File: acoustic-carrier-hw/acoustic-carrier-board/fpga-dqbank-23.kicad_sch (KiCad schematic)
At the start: 32 parts, among them IC1 ECP5-BGA256

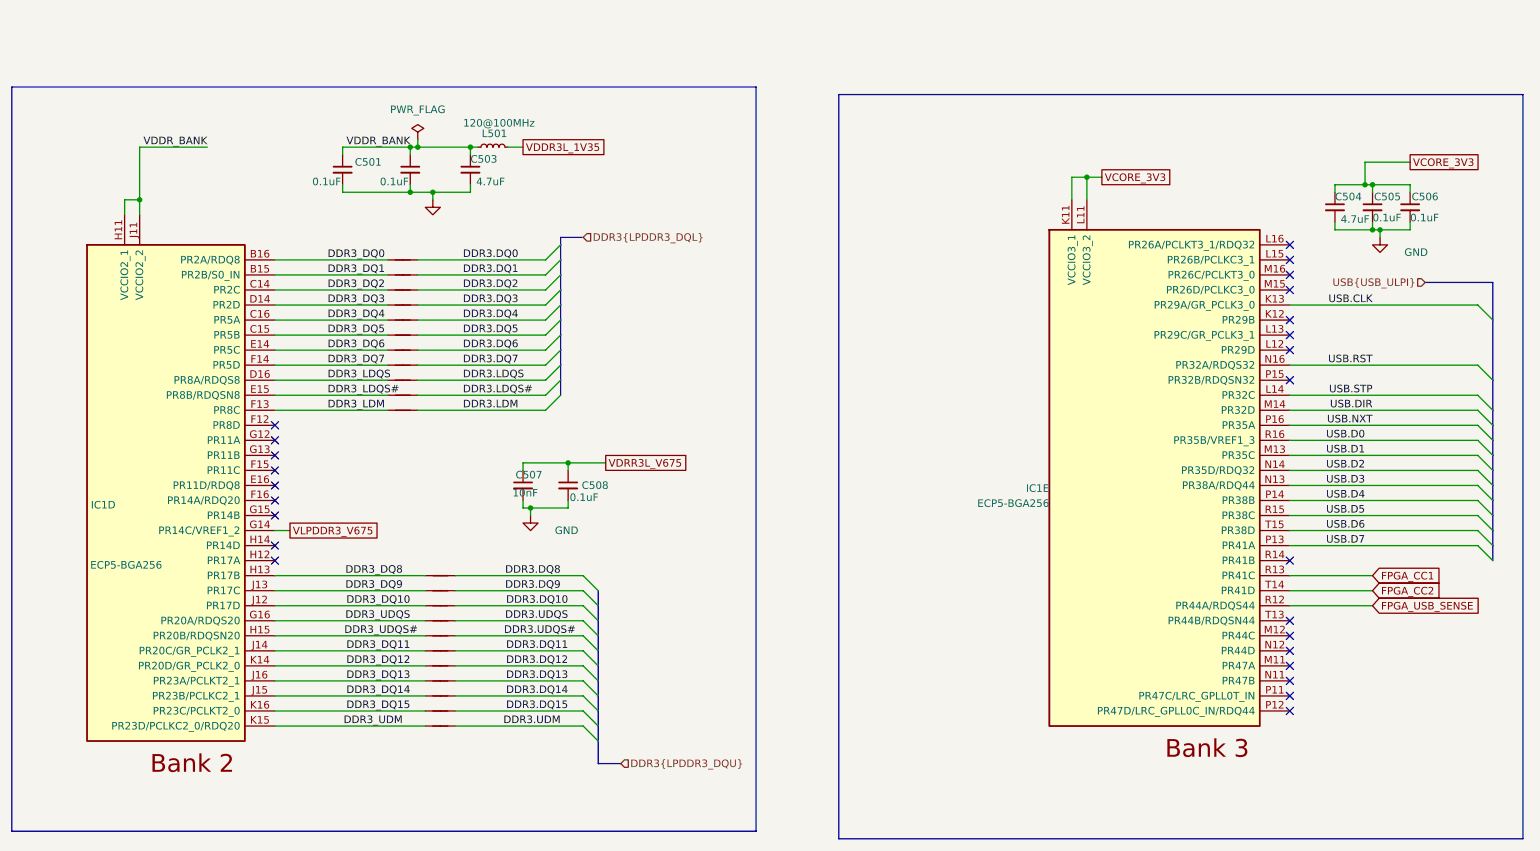
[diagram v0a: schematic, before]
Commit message: [carrier] Removed USB-switch, placed decouplpling for DDR3 and ECP5U (next) consider adding buffers on CC1 and CC2 pins
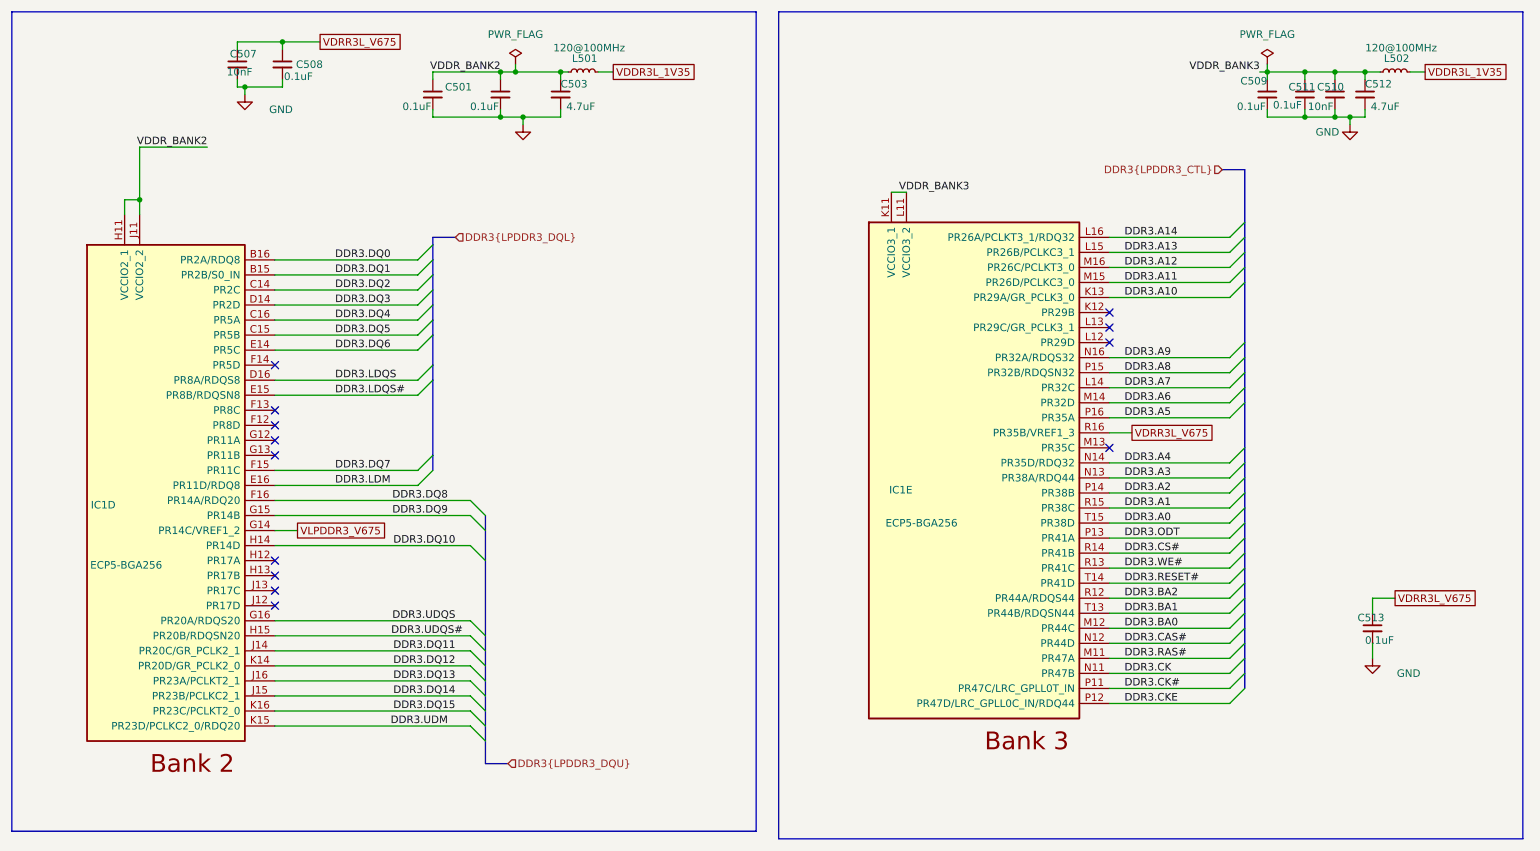
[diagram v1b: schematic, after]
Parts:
- removed C504: 4.7uF, Capacitor_SMD:C_0402_1005Metric, symbol Device:C_Small
- removed C505, C506: 0.1uF, Capacitor_SMD:C_0402_1005Metric, symbol Device:C_Small
- removed NT502, NT503, NT504, NT507, NT508, NT509, NT510, NT511, NT513, NT514, NT515, NT516, NT517, NT518, NT519, NT520, NT523, NT524: NetTie_2, iw-misc:NetTie-2_SMD_Pad0.1565mm, symbol Device:NetTie_2
- removed NT505, NT506, NT521, NT522: NetTie_2, iw-misc:NetTie-2_SMD_Pad0.1240mm, symbol Device:NetTie_2
- added C509, C510, C513: 0.1uF, Capacitor_SMD:C_0201_0603Metric, symbol Device:C_Small
- added C511: 10nF, Capacitor_SMD:C_0201_0603Metric, symbol Device:C_Small
- added C512: 4.7uF, Capacitor_SMD:C_0402_1005Metric, symbol Device:C_Small
- added L502: 120@100MHz, Inductor_SMD:L_0603_1608Metric, symbol Device:L_Small
- C501, C502, C508: footprint Capacitor_SMD:C_0402_1005Metric -> Capacitor_SMD:C_0201_0603Metric; LPN C307331 -> C22435929; MPN CL05B104KB54PNC -> CGA0201X7R104K160ET
- C507: footprint Capacitor_SMD:C_0402_1005Metric -> Capacitor_SMD:C_0201_0603Metric; LPN C15195 -> C285010; MPN CL05B103KB5NNNC -> 0201B103K250NT
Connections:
- net DDR3_DQ0 is gone; now on net DDR3.DQ0: IC1.B16 (PR2A/RDQ8)
- net DDR3_DQ1 is gone; now on net DDR3.DQ1: IC1.B15 (PR2B/S0_IN)
- net DDR3_DQ11 is gone; now on net DDR3.DQ11: IC1.J14 (PR20C/GR_PCLK2_1)
- net DDR3_DQ12 is gone; now on net DDR3.DQ12: IC1.K14 (PR20D/GR_PCLK2_0)
- net DDR3_DQ13 is gone; now on net DDR3.DQ13: IC1.J16 (PR23A/PCLKT2_1)
- net DDR3_DQ14 is gone; now on net DDR3.DQ14: IC1.J15 (PR23B/PCLKC2_1)
- net DDR3_DQ15 is gone; now on net DDR3.DQ15: IC1.K16 (PR23C/PCLKT2_0)
- net DDR3_DQ2 is gone; now on net DDR3.DQ2: IC1.C14 (PR2C)
- net DDR3_DQ3 is gone; now on net DDR3.DQ3: IC1.D14 (PR2D)
- net DDR3_DQ4 is gone; now on net DDR3.DQ4: IC1.C16 (PR5A)
- net DDR3_DQ5 is gone; now on net DDR3.DQ5: IC1.C15 (PR5B)
- net DDR3_DQ6 is gone; now on net DDR3.DQ6: IC1.E14 (PR5C)
- net DDR3_LDQS is gone; now on net DDR3.LDQS: IC1.D16 (PR8A/RDQS8)
- net DDR3_LDQS# is gone; now on net DDR3.LDQS#: IC1.E15 (PR8B/RDQSN8)
- net DDR3_UDM is gone; now on net DDR3.UDM: IC1.K15 (PR23D/PCLKC2_0/RDQ20)
- net DDR3_UDQS is gone; now on net DDR3.UDQS: IC1.G16 (PR20A/RDQS20)
- net DDR3_UDQS# is gone; now on net DDR3.UDQS#: IC1.H15 (PR20B/RDQSN20)
- net USB.D0 is gone; now on net VDRR3L_V675: IC1.R16 (PR35B/VREF1_3)
- net DDR3.DQ10: now also IC1.H14 (PR14D)
- net DDR3.DQ7: now also IC1.F15 (PR11C)
- net DDR3.DQ8: now also IC1.F16 (PR14A/RDQ20)
- net DDR3.DQ9: now also IC1.G15 (PR14B)
- net DDR3.LDM: now also IC1.E16 (PR11D/RDQ8)
- net GND: now also C509.2, C510.2, C511.2, C512.2, C513.2
- net VDDR3L_1V35: now also L502.2
- net VDRR3L_V675: now also C513.1
- net DDR3.A13: now reaches IC1.L15 (PR26B/PCLKC3_1)
- net DDR3.A14: now reaches IC1.L16 (PR26A/PCLKT3_1/RDQ32)
- net DDR3.RAS#: now reaches IC1.M11 (PR47A)
- net DDR3.BA0: now reaches IC1.M12 (PR44C)
- net DDR3.A11: now reaches IC1.M15 (PR26D/PCLKC3_0)
- net DDR3.A12: now reaches IC1.M16 (PR26C/PCLKT3_0)
- net DDR3.CK: now reaches IC1.N11 (PR47B)
- net DDR3.CAS#: now reaches IC1.N12 (PR44D)
- net DDR3.CK#: now reaches IC1.P11 (PR47C/LRC_GPLL0T_IN)
- net DDR3.CKE: now reaches IC1.P12 (PR47D/LRC_GPLL0C_IN/RDQ44)
- net DDR3.A8: now reaches IC1.P15 (PR32B/RDQSN32)
- net DDR3.CS#: now reaches IC1.R14 (PR41B)
- net DDR3.BA1: now reaches IC1.T13 (PR44B/RDQSN44)
- net DDR3_DQ10: no longer names the net of IC1.J12 (PR17D)
- net DDR3_DQ7: no longer names the net of IC1.F14 (PR5D)
- net DDR3_DQ8: no longer names the net of IC1.H13 (PR17B)
- net DDR3_DQ9: no longer names the net of IC1.J13 (PR17C)
- net DDR3_LDM: no longer names the net of IC1.F13 (PR8C)
- net FPGA_CC1 renamed DDR3.WE#
- net FPGA_CC2 renamed DDR3.RESET#
- net FPGA_USB_SENSE renamed DDR3.BA2
- net USB.CLK renamed DDR3.A10
- net USB.D1: no longer names the net of IC1.M13 (PR35C)
- net USB.D2 renamed DDR3.A4
- net USB.D3 renamed DDR3.A3
- net USB.D4 renamed DDR3.A2
- net USB.D5 renamed DDR3.A1
- net USB.D6 renamed DDR3.A0
- net USB.D7 renamed DDR3.ODT
- net USB.DIR renamed DDR3.A6
- net USB.NXT renamed DDR3.A5
- net USB.RST renamed DDR3.A9
- net USB.STP renamed DDR3.A7
- net VCORE_3V3 renamed VDDR_BANK3
- net VDDR_BANK3: now also C509.1, C510.1, C511.1, C512.1, L502.1
- net VDDR_BANK renamed VDDR_BANK2
- no-connect marks 25 -> 13
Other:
- moved on the sheet: C501, C503, C507, C508, IC1E, L501

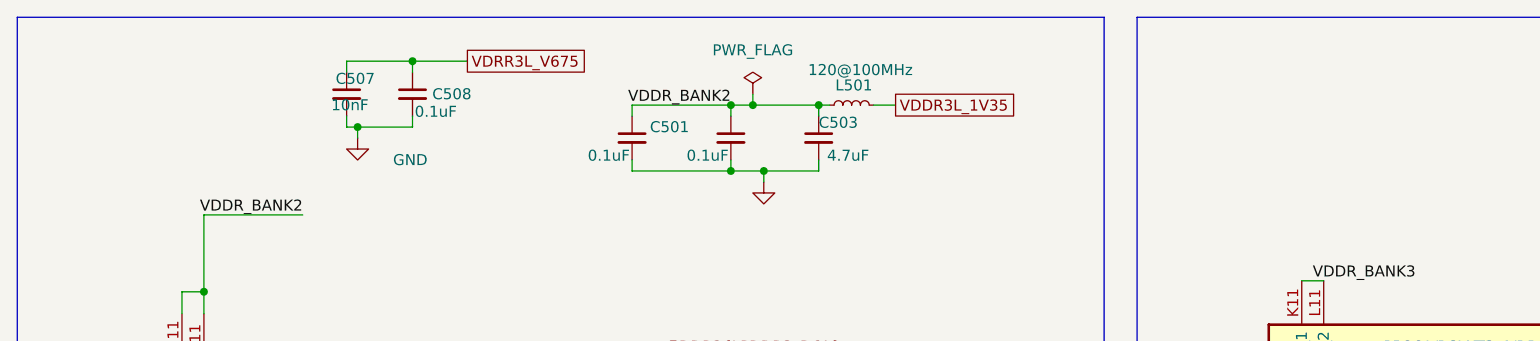
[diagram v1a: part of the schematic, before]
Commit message: [carrier] connected ethernet, usb and adc to appropriate banks, redpositioned schmitt trigger and USB
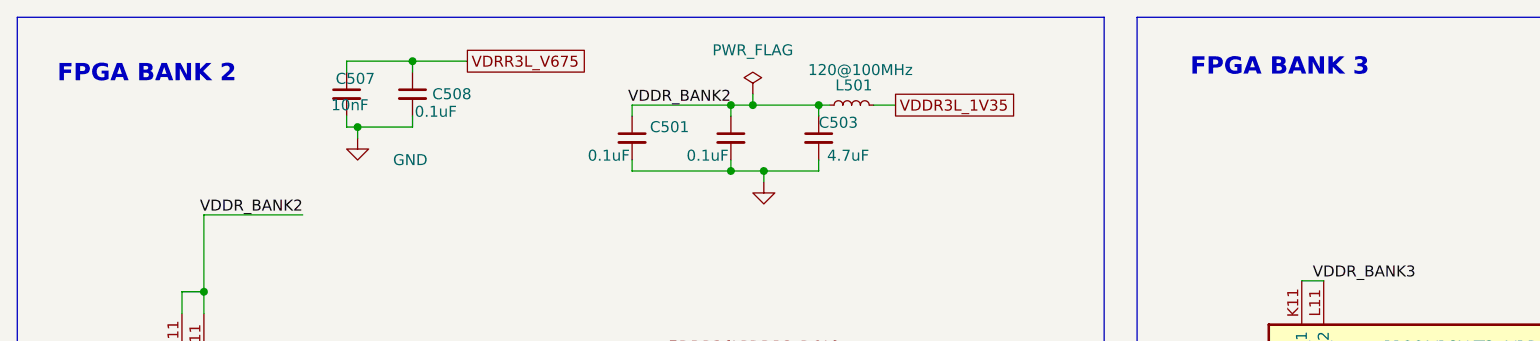
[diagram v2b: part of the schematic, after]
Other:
- note added: "FPGA BANK 2"
- note added: "FPGA BANK 3"
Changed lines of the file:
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@@
+		)
+	)
+	(text "FPGA BANK 3\n"
+		(exclude_from_sim no)
+		(at 172.72 26.162 0)
+		(effects
+			(font
+				(size 2 2)
+				(thickness 0.254)
+				(bold yes)
+			)
+		)
+	)
+	(text "FPGA BANK 2"
+		(exclude_from_sim no)
+		(at 41.656 26.924 0)
+		(effects
+			(font
+				(size 2 2)
+				(thickness 0.254)
+				(bold yes)
+			)
 		)
 	)

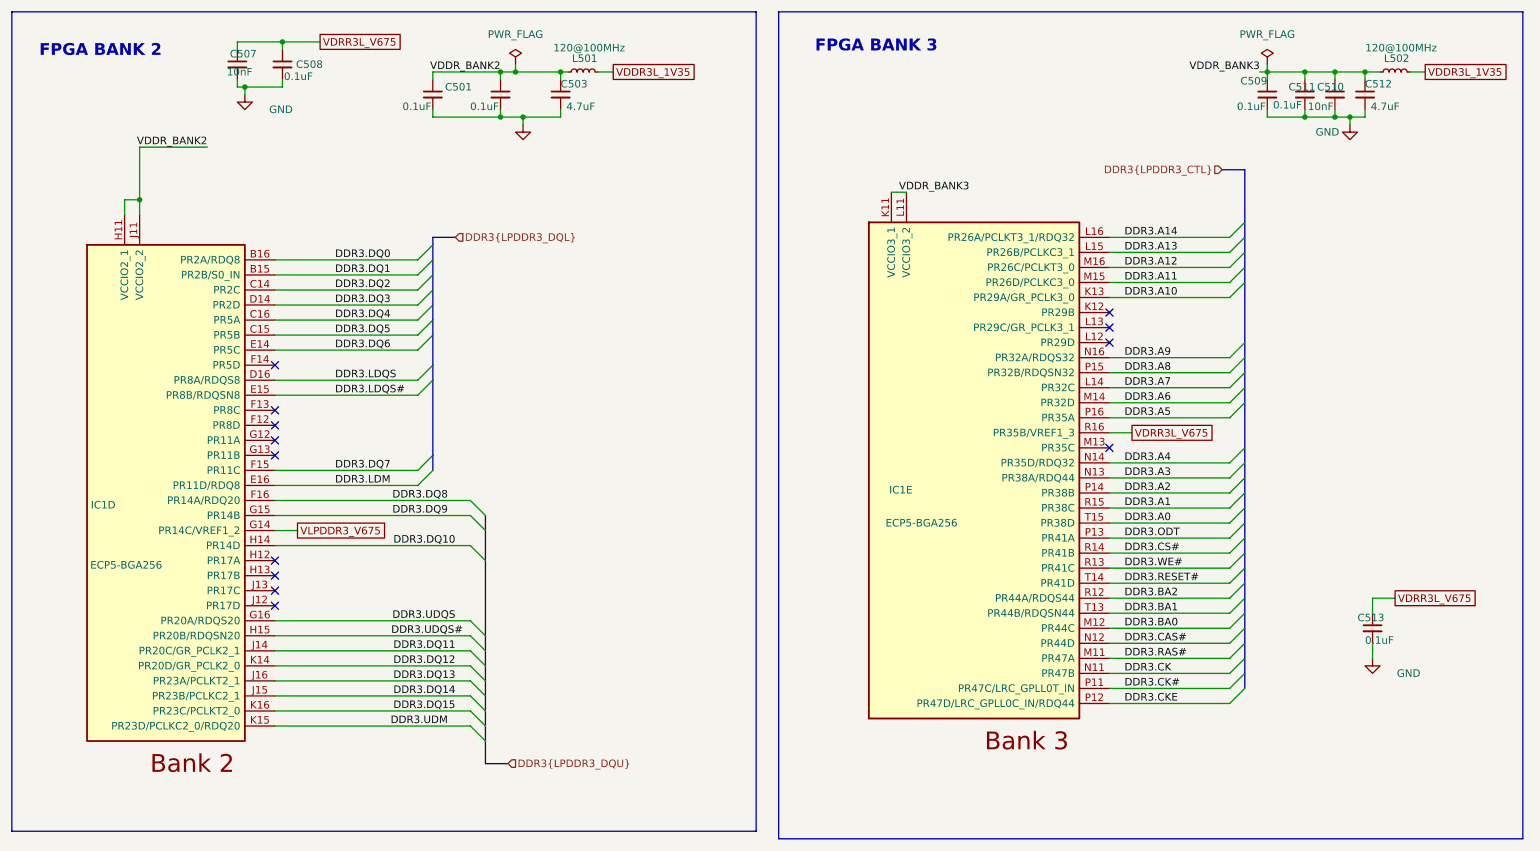
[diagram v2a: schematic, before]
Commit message: [carrier] trying horizontal layout
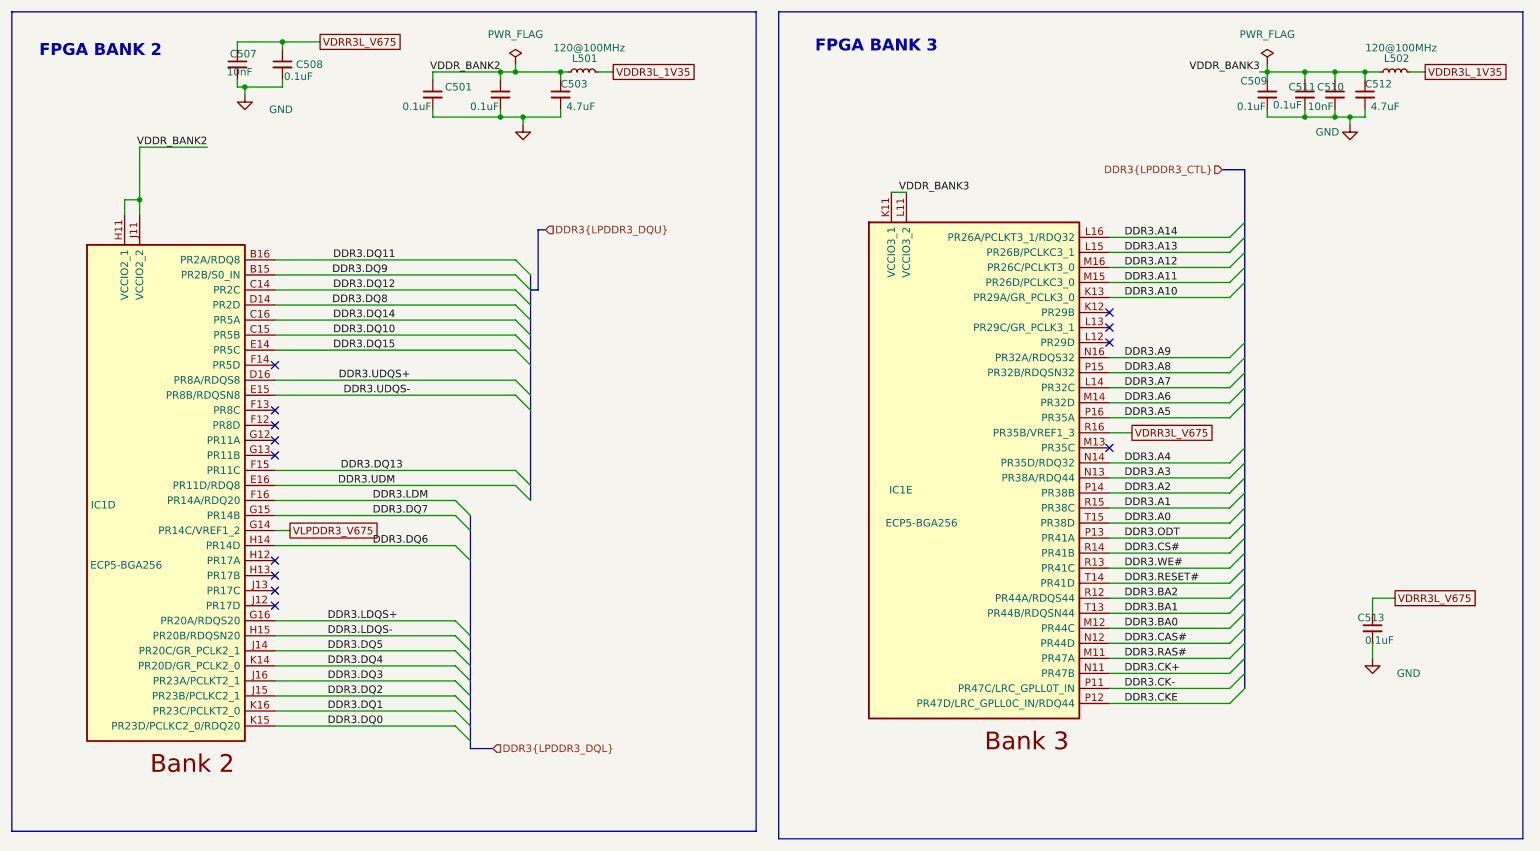
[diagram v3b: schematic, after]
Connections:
- net DDR3.DQ0: now also IC1.K15 (PR23D/PCLKC2_0/RDQ20); no longer IC1.B16 (PR2A/RDQ8)
- net DDR3.DQ1: now also IC1.K16 (PR23C/PCLKT2_0); no longer IC1.B15 (PR2B/S0_IN)
- net DDR3.DQ10: now also IC1.C15 (PR5B); no longer IC1.H14 (PR14D)
- net DDR3.DQ11: now also IC1.B16 (PR2A/RDQ8); no longer IC1.J14 (PR20C/GR_PCLK2_1)
- net DDR3.DQ12: now also IC1.C14 (PR2C); no longer IC1.K14 (PR20D/GR_PCLK2_0)
- net DDR3.DQ13: now also IC1.F15 (PR11C); no longer IC1.J16 (PR23A/PCLKT2_1)
- net DDR3.DQ14: now also IC1.C16 (PR5A); no longer IC1.J15 (PR23B/PCLKC2_1)
- net DDR3.DQ15: now also IC1.E14 (PR5C); no longer IC1.K16 (PR23C/PCLKT2_0)
- net DDR3.DQ2: now also IC1.J15 (PR23B/PCLKC2_1); no longer IC1.C14 (PR2C)
- net DDR3.DQ3: now also IC1.J16 (PR23A/PCLKT2_1); no longer IC1.D14 (PR2D)
- net DDR3.DQ4: now also IC1.K14 (PR20D/GR_PCLK2_0); no longer IC1.C16 (PR5A)
- net DDR3.DQ5: now also IC1.J14 (PR20C/GR_PCLK2_1); no longer IC1.C15 (PR5B)
- net DDR3.DQ6: now also IC1.H14 (PR14D); no longer IC1.E14 (PR5C)
- net DDR3.DQ7: now also IC1.G15 (PR14B); no longer IC1.F15 (PR11C)
- net DDR3.DQ8: now also IC1.D14 (PR2D); no longer IC1.F16 (PR14A/RDQ20)
- net DDR3.DQ9: now also IC1.B15 (PR2B/S0_IN); no longer IC1.G15 (PR14B)
- net DDR3.LDM: now also IC1.F16 (PR14A/RDQ20); no longer IC1.E16 (PR11D/RDQ8)
- net DDR3.UDM: now also IC1.E16 (PR11D/RDQ8); no longer IC1.K15 (PR23D/PCLKC2_0/RDQ20)
- net DDR3.CK renamed DDR3.CK+
- net DDR3.CK# renamed DDR3.CK-
- net DDR3.LDQS renamed DDR3.UDQS+
- net DDR3.LDQS# renamed DDR3.UDQS-
- net DDR3.UDQS renamed DDR3.LDQS+
- net DDR3.UDQS# renamed DDR3.LDQS-

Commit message: [carrier] Connected the pins to the DDR3 (next) reorient the pins so the first array goes around the DDR3 memory on the first layer, connecting to the back of the BGA
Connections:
- net DDR3.A0: no longer IC1.T15 (PR38D)
- net DDR3.A1: now also IC1.T15 (PR38D); no longer IC1.R15 (PR38C)
- net DDR3.A10: now also IC1.P15 (PR32B/RDQSN32); no longer IC1.K13 (PR29A/GR_PCLK3_0)
- net DDR3.A11: now also IC1.T14 (PR41D); no longer IC1.M15 (PR26D/PCLKC3_0)
- net DDR3.A12: now also IC1.R15 (PR38C); no longer IC1.M16 (PR26C/PCLKT3_0)
- net DDR3.A14: now also IC1.T13 (PR44B/RDQSN44); no longer IC1.L16 (PR26A/PCLKT3_1/RDQ32)
- net DDR3.A4: now also IC1.P13 (PR41A); no longer IC1.N14 (PR35D/RDQ32)
- net DDR3.A6: now also IC1.R13 (PR41C); no longer IC1.M14 (PR32D)
- net DDR3.A8: now also IC1.R12 (PR44A/RDQS44); no longer IC1.P15 (PR32B/RDQSN32)
- net DDR3.BA1: now also IC1.R14 (PR41B); no longer IC1.T13 (PR44B/RDQSN44)
- net DDR3.BA2: no longer IC1.R12 (PR44A/RDQS44)
- net DDR3.CS#: no longer IC1.R14 (PR41B)
- net DDR3.ODT: no longer IC1.P13 (PR41A)
- net DDR3.RESET#: no longer IC1.T14 (PR41D)
- net DDR3.WE#: no longer IC1.R13 (PR41C)
